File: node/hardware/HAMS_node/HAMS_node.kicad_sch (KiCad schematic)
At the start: 26 parts, among them J1 Conn_02x04_Counter_Clockwise, J2 Conn_02x07_Odd_Even, J3 Screw_Terminal_01x02, J4 Conn_02x04_Odd_Even, J5 Conn_01x06, Q1 PMOS, Y1 CM9V-T1A-32.768KHZ-7PF-20PPM-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

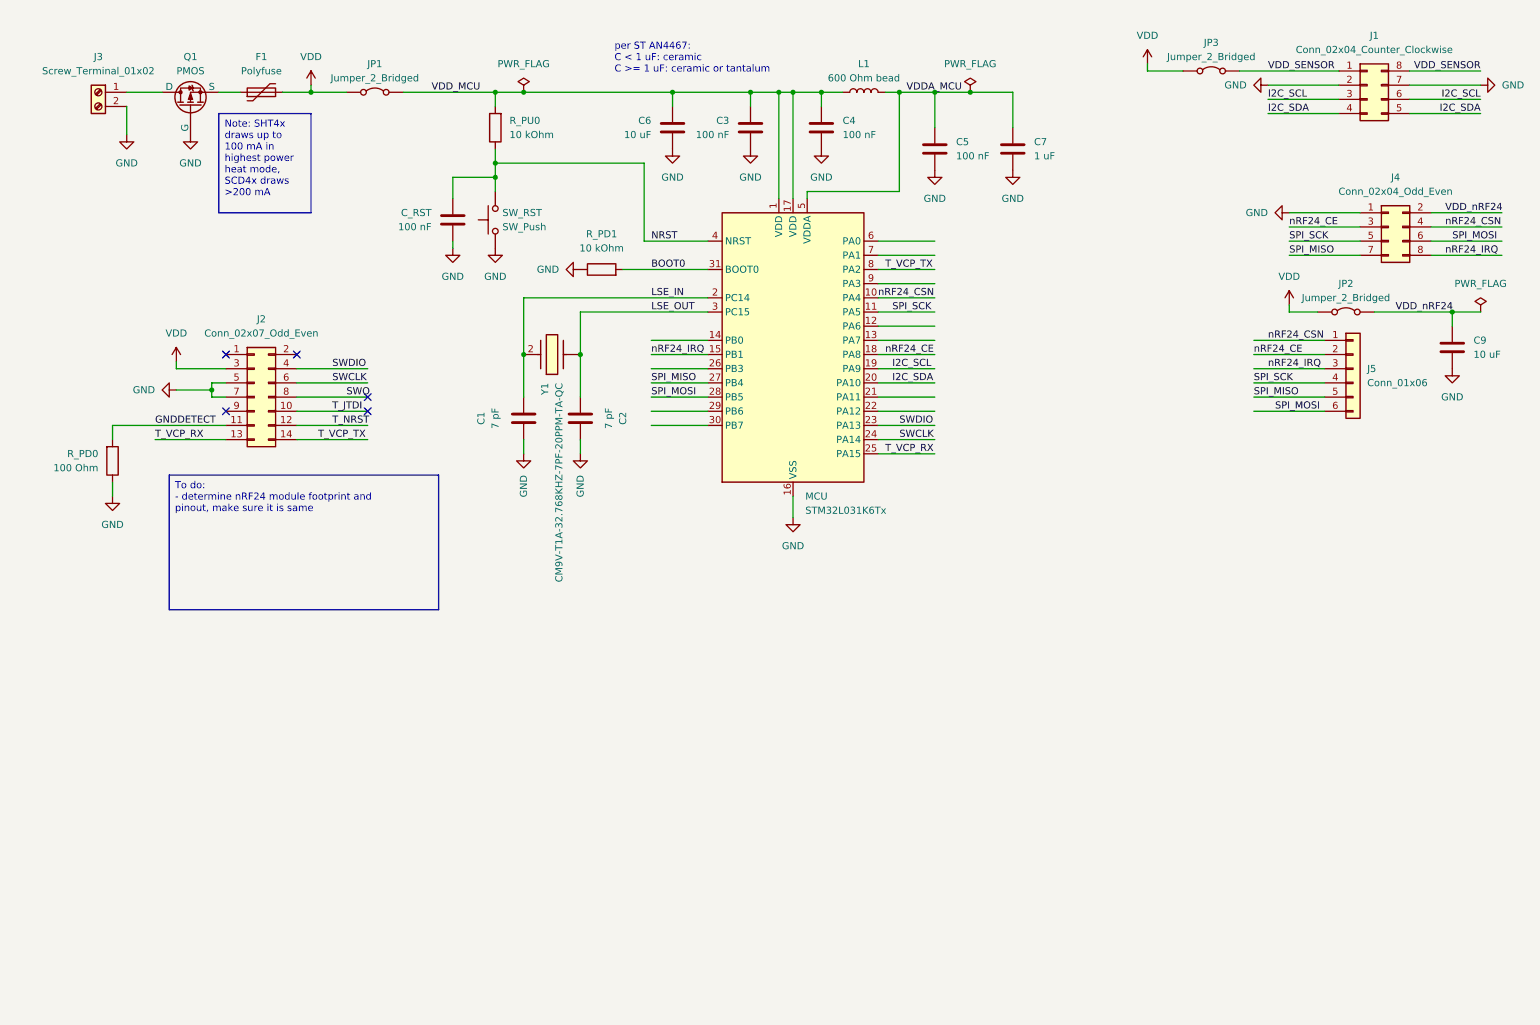
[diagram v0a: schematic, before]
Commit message: Improve HAMS node HW: add WIP PCB, edit schematic
Update schematic significantly (adding nRF24 modules, specify parts, add
notes etc).
Add preliminary PCB layout (WIP).
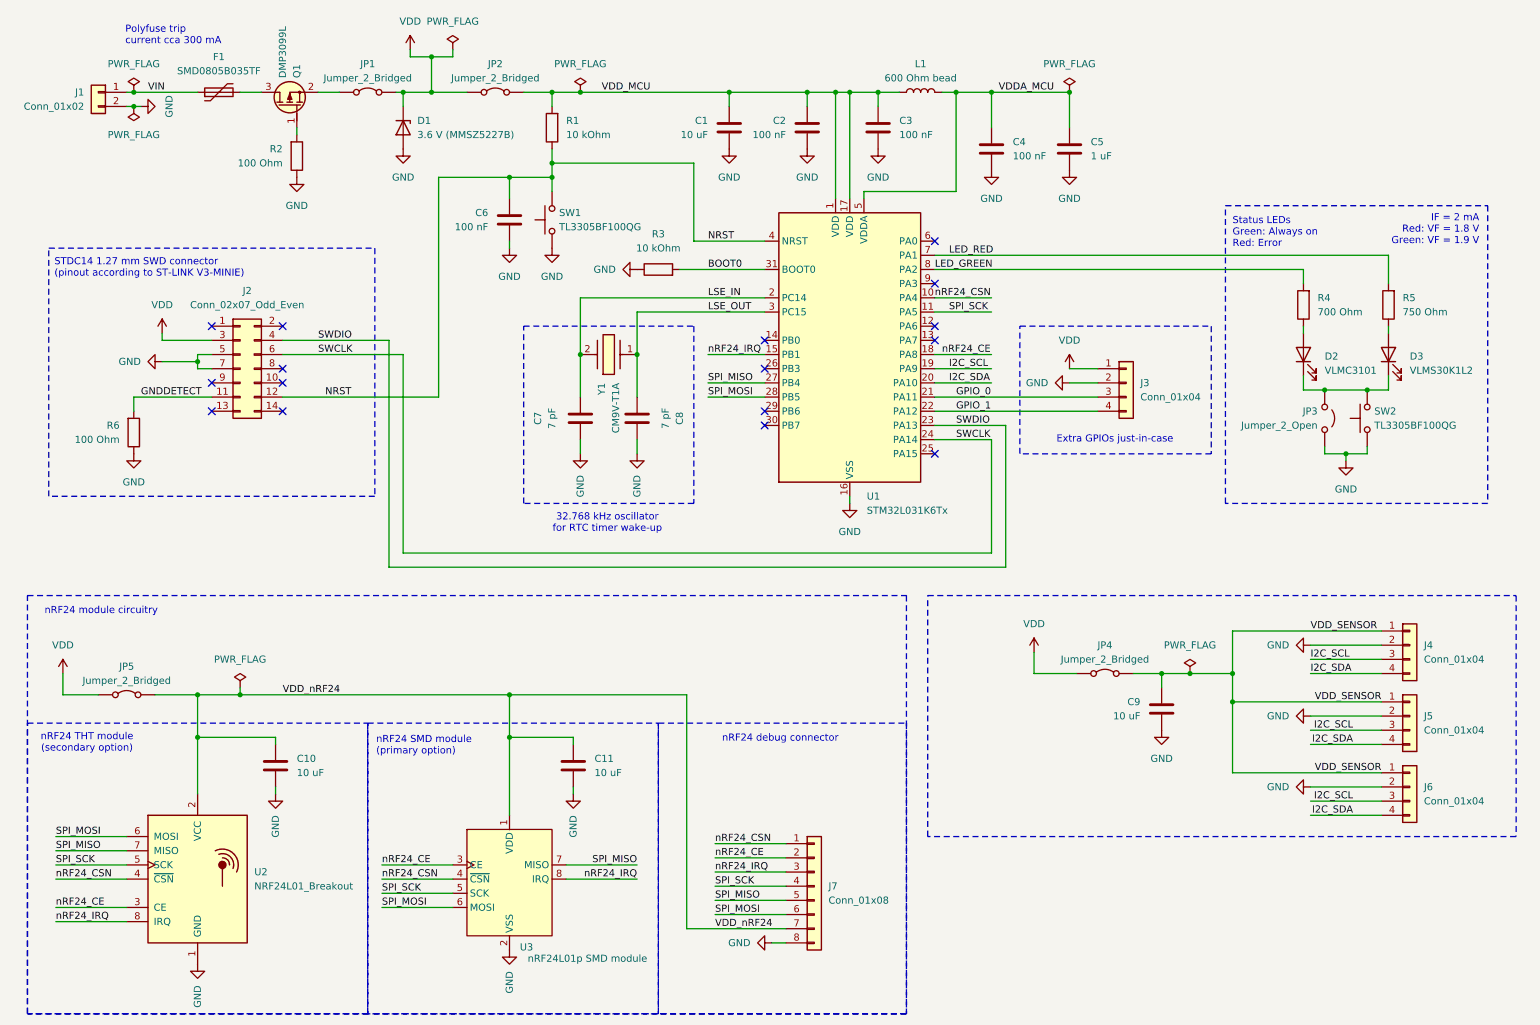
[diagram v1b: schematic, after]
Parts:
- removed J1: Conn_02x04_Counter_Clockwise, symbol Connector_Generic:Conn_02x04_Counter_Clockwise
- removed J3: Screw_Terminal_01x02, symbol Connector:Screw_Terminal_01x02
- removed J4: Conn_02x04_Odd_Even, Connector_PinHeader_2.54mm:PinHeader_2x04_P2.54mm_Vertical, symbol Connector_Generic:Conn_02x04_Odd_Even
- removed J5: Conn_01x06, symbol Connector_Generic:Conn_01x06
- removed Q1: PMOS, symbol Simulation_SPICE:PMOS
- added C10, C11: 10 uF, Capacitor_SMD:C_0805_2012Metric_Pad1.18x1.45mm_HandSolder, symbol Device:C
- added D1: 3.6 V (MMSZ5227B), PCM_Diode_SMD_Handsoldering_AKL:D_SOD-123_Zener, symbol Device:D_Zener
- added D2: VLMC3101, LED_SMD:LED_PLCC-2_3.4x3.0mm_KA, symbol Device:LED
- added D3: VLMS30K1L2, LED_SMD:LED_PLCC-2_3.4x3.0mm_KA, symbol Device:LED
- added J1: Conn_01x02, Connector_PinSocket_2.54mm:PinSocket_1x02_P2.54mm_Horizontal, symbol Connector_Generic:Conn_01x02
- added J3, J6: Conn_01x04, Connector_PinSocket_2.54mm:PinSocket_1x04_P2.54mm_Vertical, symbol Connector_Generic:Conn_01x04
- added J4, J5: Conn_01x04, Connector_PinSocket_2.54mm:PinSocket_1x04_P2.54mm_Horizontal, symbol Connector_Generic:Conn_01x04
- added J7: Conn_01x08, Connector_PinSocket_2.54mm:PinSocket_1x08_P2.54mm_Vertical, symbol Connector_Generic:Conn_01x08
- added JP1: Jumper_2_Bridged, Connector_PinHeader_2.54mm:PinHeader_2x01_P2.54mm_Vertical, symbol Jumper:Jumper_2_Bridged
- added JP3: Jumper_2_Open, Connector_PinHeader_2.54mm:PinHeader_2x01_P2.54mm_Vertical, symbol Jumper:Jumper_2_Open
- added Q1: DMP3099L, PCM_Package_TO_SOT_SMD_AKL:SOT-23, symbol PCM_Transistor_MOSFET_AKL:DMP3099L
- added R2: 100 Ohm, Resistor_SMD:R_0805_2012Metric_Pad1.20x1.40mm_HandSolder, symbol Device:R
- added R4: 700 Ohm, Resistor_SMD:R_0805_2012Metric_Pad1.20x1.40mm_HandSolder, symbol Device:R
- added R5: 750 Ohm, Resistor_SMD:R_0805_2012Metric_Pad1.20x1.40mm_HandSolder, symbol Device:R
- added SW2: TL3305BF100QG, Personal_Switches:E-Switch_TL3305BF100QG_Tactile_SPST, symbol Switch:SW_Push
- added U2: NRF24L01_Breakout, RF_Module:nRF24L01_Breakout, symbol RF:NRF24L01_Breakout
- added U3: nRF24L01p SMD module, Personal_Modules:nRF24L01p_SMD_module, symbol Personal_Modules:nRF24L01p_SMD_module
- C1: renamed from C6; footprint (none) -> Capacitor_SMD:C_0805_2012Metric_Pad1.18x1.45mm_HandSolder
- C2: renamed from C3; footprint (none) -> Capacitor_SMD:C_0805_2012Metric_Pad1.18x1.45mm_HandSolder
- C3: renamed from C4; footprint (none) -> Capacitor_SMD:C_0805_2012Metric_Pad1.18x1.45mm_HandSolder
- C4: renamed from C5; footprint (none) -> Capacitor_SMD:C_0805_2012Metric_Pad1.18x1.45mm_HandSolder
- C5: renamed from C7; footprint (none) -> Capacitor_SMD:C_0805_2012Metric_Pad1.18x1.45mm_HandSolder
- C6: renamed from C_RST; footprint (none) -> Capacitor_SMD:C_0805_2012Metric_Pad1.18x1.45mm_HandSolder
- C7: renamed from C1; footprint (none) -> Capacitor_SMD:C_0805_2012Metric_Pad1.18x1.45mm_HandSolder
- C8: renamed from C2; footprint (none) -> Capacitor_SMD:C_0805_2012Metric_Pad1.18x1.45mm_HandSolder
- C9: footprint (none) -> Capacitor_SMD:C_0805_2012Metric_Pad1.18x1.45mm_HandSolder
- F1: value Polyfuse -> SMD0805B035TF; footprint (none) -> Personal_Fuses:YAGEO_SMD0805_Fuse
- J2: footprint (none) -> Connector_PinHeader_1.27mm:PinHeader_2x07_P1.27mm_Vertical_SMD
- JP2: renamed from JP1; footprint (none) -> Connector_PinHeader_2.54mm:PinHeader_2x01_P2.54mm_Vertical
- JP4: renamed from JP3; footprint (none) -> Connector_PinHeader_2.54mm:PinHeader_2x01_P2.54mm_Vertical
- JP5: renamed from JP2; footprint (none) -> Connector_PinHeader_2.54mm:PinHeader_2x01_P2.54mm_Vertical
- L1: footprint (none) -> Inductor_SMD:L_0805_2012Metric_Pad1.15x1.40mm_HandSolder
- R1: renamed from R_PU0; footprint (none) -> Resistor_SMD:R_0805_2012Metric_Pad1.20x1.40mm_HandSolder
- R3: renamed from R_PD1; footprint (none) -> Resistor_SMD:R_0805_2012Metric_Pad1.20x1.40mm_HandSolder
- R6: renamed from R_PD0; footprint (none) -> Resistor_SMD:R_0805_2012Metric_Pad1.20x1.40mm_HandSolder
- SW1: renamed from SW_RST; value SW_Push -> TL3305BF100QG; footprint (none) -> Personal_Switches:E-Switch_TL3305BF100QG_Tactile_SPST
- Y1: value CM9V-T1A-32.768KHZ-7PF-20PPM-TA-QC -> CM9V-T1A; footprint CM9VT1A -> PCM_Crystal_Handsoldering_AKL:Crystal_SMD_MicroCrystal_CM9V-T1A-2Pin_1.6x1.0mm_BigPads
- renumbered MCU to U1
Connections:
- net T_NRST is gone; now on net NRST: J2.12 (Pin_12)
- net GND: now also C10.1, C11.1, D1.2 (A), J1.2 (Pin_2), J3.2 (Pin_2), J4.2 (Pin_2), J5.2 (Pin_2), J6.2 (Pin_2), J7.8 (Pin_8), JP3.1 (A), R2.1, SW2.1, U2.1 (GND), U3.2 (VSS)
- net I2C_SCL: now also J4.3 (Pin_3), J5.3 (Pin_3), J6.3 (Pin_3)
- net I2C_SDA: now also J4.4 (Pin_4), J5.4 (Pin_4), J6.4 (Pin_4)
- net LSE_OUT: now also Y1.1 (X1); no longer Y1.
- net SPI_MISO: now also J7.5 (Pin_5), U2.7 (MISO), U3.7 (MISO)
- net SPI_MOSI: now also J7.6 (Pin_6), U2.6 (MOSI), U3.6 (MOSI)
- net SPI_SCK: now also J7.4 (Pin_4), U2.5 (SCK), U3.5 (SCK)
- net VDD: now also D1.1 (K), J3.1 (Pin_1), JP1.2 (B); no longer F1.2
- net VDD_SENSOR: now also C9.1, J4.1 (Pin_1), J5.1 (Pin_1), J6.1 (Pin_1)
- net VDD_nRF24: now also C10.2, C11.2, J7.7 (Pin_7), U2.2 (VCC), U3.1 (VDD); no longer C9.1
- net nRF24_CE: now also J7.2 (Pin_2), U2.3 (CE), U3.3 (CE)
- net nRF24_CSN: now also J7.1 (Pin_1), U2.4 (~{CSN}), U3.4 (~{CSN})
- net nRF24_IRQ: now also J7.3 (Pin_3), U2.8 (IRQ), U3.8 (IRQ)
- net VIN: now reaches F1.1
- net VIN: now also J1.1 (Pin_1)
- net GPIO_0: now reaches U1.21 (PA11)
- net GPIO_0: now also J3.3 (Pin_3)
- net GPIO_1: now reaches U1.22 (PA12)
- net GPIO_1: now also J3.4 (Pin_4)
- net LED_RED: now reaches U1.7 (PA1)
- net LED_RED: now also R5.2
- net SWO: no longer names the net of J2.8 (Pin_8)
- net T_JTDI: no longer names the net of J2.10 (Pin_10)
- net T_VCP_RX: no longer names the net of J2.13 (Pin_13)
- net T_VCP_RX: no longer U1.25 (PA15)
- net T_VCP_TX: no longer names the net of J2.14 (Pin_14)
- net T_VCP_TX: no longer U1.8 (PA2)
- new net: D2.1 (K), D3.1 (K), JP3.2 (B), SW2.2
- new net: D2.2 (A), R4.1
- new net: Q1.1 (G), R2.2
- new net: JP1.1 (A), Q1.2 (S)
- new net: F1.2, Q1.3 (D)
- new net: D3.2 (A), R5.1
- new net LED_GREEN: R4.2, U1.8 (PA2)
- no-connect marks 5 -> 16
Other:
- note added: "32.768 kHz oscillator for RTC timer wake-up"
- note added: "Extra GPIOs just-in-case"
- note added: "IF = 2 mA Red: VF = 1.8 V Green: VF = 1.9 V"
- note added: "Polyfuse trip current cca 300 mA"
- note added: "STDC14 1.27 mm SWD connector (pinout according to ST-LINK V3-MINIE)"
- note added: "Status LEDs Green: Always on Red: Error"
- note added: "nRF24 SMD module (primary option)"
- note added: "nRF24 THT module (secondary option)"
- note added: "nRF24 debug connector"
- note added: "nRF24 module circuitry"
- moved on the sheet: C1, C2, C3, C4, C5, C6, C7, C8, F1, J2, JP2, JP4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

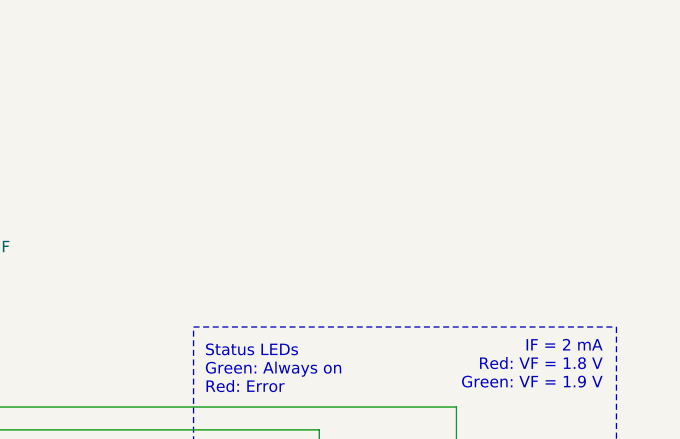
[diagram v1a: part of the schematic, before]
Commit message: Improve HAMS node HW: PCB and device resize
Change many 0805 devices for 0603 devices.
Add mounting holes.
Make the board 4.5 x 5 cm size.
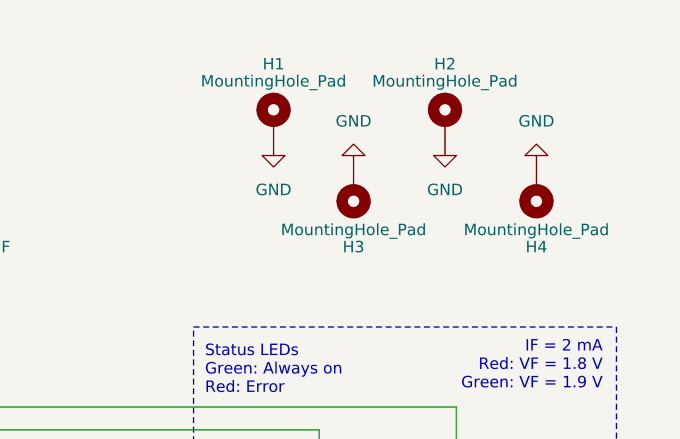
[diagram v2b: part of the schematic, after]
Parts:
- added H1, H2, H3, H4: MountingHole_Pad, MountingHole:MountingHole_2.2mm_M2_ISO7380_Pad_TopBottom, symbol Mechanical:MountingHole_Pad
- C1, C10, C11, C2, C3, C4, C5, C6, C7, C8, C9: footprint Capacitor_SMD:C_0805_2012Metric_Pad1.18x1.45mm_HandSolder -> Capacitor_SMD:C_0603_1608Metric_Pad1.08x0.95mm_HandSolder
- L1: footprint Inductor_SMD:L_0805_2012Metric_Pad1.15x1.40mm_HandSolder -> Inductor_SMD:L_0603_1608Metric_Pad1.05x0.95mm_HandSolder
- R1, R2, R3, R4, R5, R6: footprint Resistor_SMD:R_0805_2012Metric_Pad1.20x1.40mm_HandSolder -> PCM_Resistor_SMD_AKL:R_0603_1608Metric_Pad1.05x0.95mm_HandSolder
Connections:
- net GND: now also H1.1, H2.1, H3.1, H4.1
